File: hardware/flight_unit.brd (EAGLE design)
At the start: 160 x 100 mm, 28 parts, among them IC2 7805T, J2 CONN_20X2SHROUDED, T1 THERMISTOR-2,5, U1 4MB Flash, U2 4MB Flash, U3 4MB Flash, X1 S4B-ZR, X2 S4B-ZR

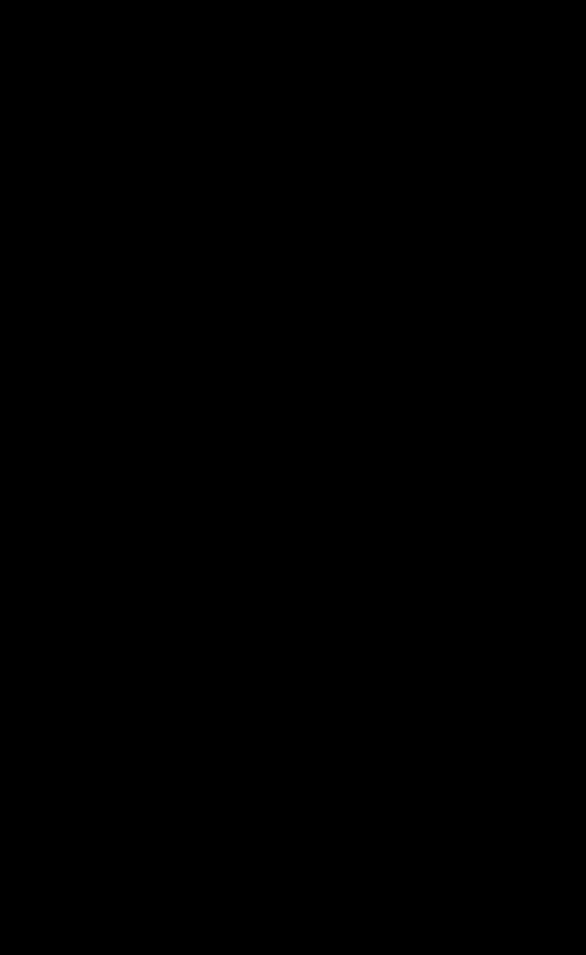
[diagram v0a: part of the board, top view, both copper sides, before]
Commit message: Added decoupling caps to memory schematic
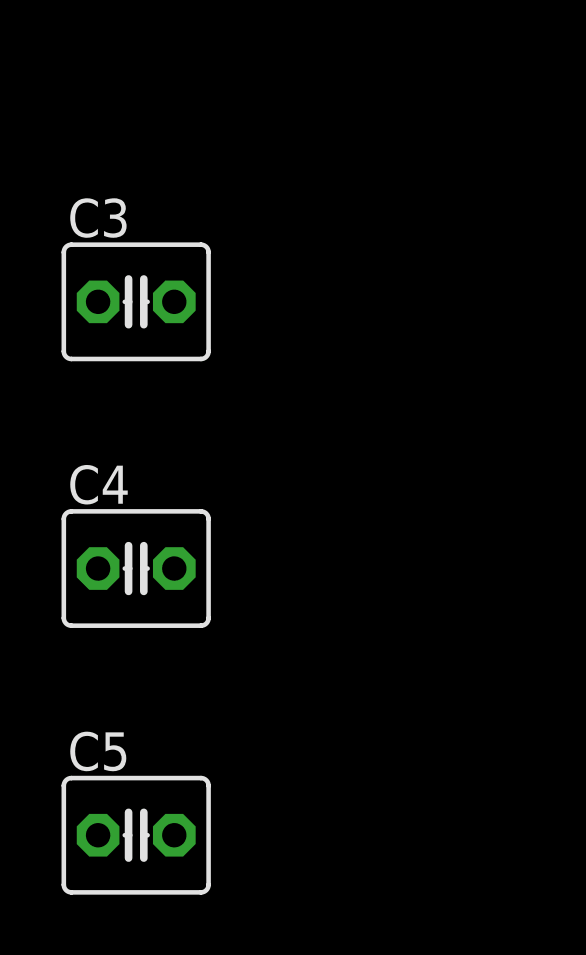
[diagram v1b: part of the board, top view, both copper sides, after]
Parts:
- added C3, C4, C5: 10uF, adafruit:C025-040X050
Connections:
- net +3V3: now also C3.1, C4.1, C5.1
- net GND: now also C3.2, C4.2, C5.2
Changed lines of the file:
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@@
 <attribute name="VALUE" x="-68.58" y="85.09" size="1.27" layer="27"/>
+</element>
+<element name="C3" library="adafruit" library_urn="urn:adsk.eagle:library:420" package="C025-040X050" package3d_urn="urn:adsk.eagle:package:6240321/1" value="10uF" x="-72.39" y="-5.08" smashed="yes">
+<attribute name="NAME" x="-74.676" y="-2.921" size="1.27" layer="25" ratio="10"/>
+<attribute name="VALUE" x="-74.676" y="-8.509" size="1.27" layer="27" ratio="10"/>
+</element>
+<element name="C4" library="adafruit" library_urn="urn:adsk.eagle:library:420" package="C025-040X050" package3d_urn="urn:adsk.eagle:package:6240321/1" value="10uF" x="-72.39" y="-13.97" smashed="yes">
+<attribute name="NAME" x="-74.676" y="-11.811" size="1.27" layer="25" ratio="10"/>
+<attribute name="VALUE" x="-74.676" y="-17.399" size="1.27" layer="27" ratio="10"/>
+</element>
+<element name="C5" library="adafruit" library_urn="urn:adsk.eagle:library:420" package="C025-040X050" package3d_urn="urn:adsk.eagle:package:6240321/1" value="10uF" x="-72.39" y="-22.86" smashed="yes">
+<attribute name="NAME" x="-74.676" y="-20.701" size="1.27" layer="25" ratio="10"/>
+<attribute name="VALUE" x="-74.676" y="-26.289" size="1.27" layer="27" ratio="10"/>
 </element>
 </elements>
@@
 <contactref element="R8" pad="1"/>
 <contactref element="U$3" pad="VIN"/>
+<contactref element="C3" pad="1"/>
+<contactref element="C4" pad="1"/>
+<contactref element="C5" pad="1"/>
 <wire x1="-27.94" y1="121.92" x2="-19.685" y2="118.37" width="0" layer="19" extent="1-1"/>
 <wire x1="-20.19" y1="107.95" x2="-19.685" y2="118.37" width="0" layer="19" extent="1-1"/>
@@
 <wire x1="-48.26" y1="64.77" x2="-70.99" y2="87.63" width="0" layer="19" extent="1-1"/>
 <wire x1="-33.655" y1="64.77" x2="-48.26" y2="64.77" width="0" layer="19" extent="1-1"/>
+<wire x1="-73.66" y1="-5.08" x2="-48.26" y2="64.77" width="0" layer="19" extent="1-1"/>
+<wire x1="-73.66" y1="-13.97" x2="-73.66" y2="-5.08" width="0" layer="19" extent="1-1"/>
+<wire x1="-73.66" y1="-22.86" x2="-73.66" y2="-13.97" width="0" layer="19" extent="1-1"/>
 </signal>
 <signal name="GND">
@@
 <contactref element="RN2" pad="5"/>
 <contactref element="U$3" pad="GND"/>
+<contactref element="C3" pad="2"/>
+<contactref element="C4" pad="2"/>
+<contactref element="C5" pad="2"/>
 <wire x1="-29.21" y1="129.54" x2="-19.05" y2="129.54" width="0" layer="19" extent="1-1"/>
 <wire x1="-31.75" y1="120.65" x2="-29.21" y2="129.54" width="0" layer="19" extent="1-1"/>
@@
 <wire x1="-48.385" y1="5.08" x2="-40.515" y2="5.08" width="0" layer="19" extent="1-1"/>
 <wire x1="-48.385" y1="10.16" x2="-48.385" y2="5.08" width="0" layer="19" extent="1-1"/>
+<wire x1="-71.12" y1="-5.08" x2="-48.385" y2="5.08" width="0" layer="19" extent="1-1"/>
+<wire x1="-71.12" y1="-13.97" x2="-71.12" y2="-5.08" width="0" layer="19" extent="1-1"/>
+<wire x1="-71.12" y1="-22.86" x2="-71.12" y2="-13.97" width="0" layer="19" extent="1-1"/>
 </signal>
 <signal name="N$4">

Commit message: updates to schematic and preliminary board work
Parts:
- removed J2: CONN_20X2SHROUDED, SparkFun-Connectors:2X20_SHROUDED
- removed R2, R3: 1k, resistor:R1210
- added J1: CONN_20X2SHROUDED, SparkFun-Connectors:2X20_SHROUDED
- moved C3 152.1 mm to (68.6, 52.1)
- moved C5 150.6 mm to (64.8, 39.4)
- moved U1 149.0 mm to (68.6, 33.0)
- moved U2 146.8 mm to (57.1, 33.0)
- moved C4 130.2 mm to (49.5, 31.8)
- moved RN2 116.6 mm to (53.3, 74.9), turned to 180 degrees
- moved RN1 113.1 mm to (68.6, 66.0), turned to 180 degrees
- moved JP1 112.5 mm to (69.8, 88.9), turned to 90 degrees
- moved U3 111.1 mm to (68.6, 45.7)
- moved C2 106.7 mm to (-160.0, 110.5)
- moved D1 106.7 mm to (-134.6, 119.4)
- moved LED0 106.7 mm to (-174.0, 125.7)
- moved LED1 106.7 mm to (-127.0, 133.3)
- moved R1 106.7 mm to (-160.0, 124.5)
- moved R5 106.7 mm to (-134.6, 111.8)
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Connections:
- removed net N$3: R2.1, U3.7
- removed net N$5: R4.1, U1.7
- removed net N$6: R3.1, U2.7
- new net HOLD_PUP: R4.1, U1.7, U2.7, U3.7
- net +3V3: no longer R2.2, R3.2
- net GND: now also J1.10, J1.13, J1.19, J1.26, J1.29, J1.33, J1.40, J1.5; no longer J2.14, J2.20, J2.25, J2.30, J2.34, J2.39, J2.6, J2.9
- net IIC_SCL: now also J1.30; no longer J2.29
- net IIC_SDA: now also J1.8; no longer J2.7
- net SC_3V3: now also J1.18, J1.2; no longer J2.1, J2.17
- net SC_5V0: now also J1.1, J1.3; no longer J2.2, J2.4
- net SC_D0: now also J1.7; no longer J2.8
- net SC_D1: now also J1.11; no longer J2.12
- net SC_D2: now also J1.15; no longer J2.16
- net SC_D3: now also J1.21; no longer J2.22
- net SC_D4: now also J1.35; no longer J2.36

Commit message: working on board layout
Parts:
- added H1, H2: SEW_HOLE, SparkFun-Retired:SIMPLE_HOLE
- moved R8 238.7 mm to (64.8, 58.4), turned to 270 degrees
- moved X1 226.6 mm to (47.0, 8.89)
- moved R1 224.3 mm to (33.0, 10.2), turned to 180 degrees
- moved D2 213.5 mm to (33.0, 5.08)
- moved C2 210.7 mm to (27.9, 15.2), turned to 90 degrees
- moved X2 208.0 mm to (17.8, 8.89)
- moved LED0 205.1 mm to (7.62, 30.5)
- moved T1 202.0 mm to (57.1, 58.4), turned to 270 degrees
- moved C1 201.6 mm to (27.9, 22.9), turned to 270 degrees
- moved LED2 184.9 mm to (16.5, 30.5)
- moved LED1 183.9 mm to (25.4, 30.5)
- moved D1 182.9 mm to (14.0, 12.7), turned to 180 degrees
- moved R7 179.8 mm to (17.8, 40.6), flipped to the bottom
- moved R6 171.5 mm to (17.8, 47.0), flipped to the bottom
- moved R5 162.8 mm to (17.8, 54.6), flipped to the bottom
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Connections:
- net GND: now also H1.P$1, H2.P$1
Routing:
- net +3V3: track 0.00 -> 167.1 mm
- net N$2: track 0.00 -> 23.7 mm
- net SC_A3: track 0.00 -> 23.3 mm
- net T_0: track 0.00 -> 23.2 mm
- net T_1: track 0.00 -> 19.8 mm
- net N$1: track 0.00 -> 16.6 mm
- net N$4: track 0.00 -> 8.22 mm
- net V_1: track 0.00 -> 4.83 mm
- net A_3: track 0.00 -> 4.83 mm
- net A_2: track 0.00 -> 4.83 mm
- net A_1: track 0.00 -> 4.83 mm
- net A_0: track 0.00 -> 4.83 mm
- added copper zone on layer 1, net GND
- added copper zone on layer 16, net GND
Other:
- board size 160 x 100 mm -> 77.5 x 74.6 mm

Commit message: working on routing...
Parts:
- added R2: 1k, resistor:R1210
- moved C3 54.1 mm to (11.4, 12.7), flipped to the bottom
- moved U1 45.5 mm to (14.0, 29.2)
- moved C1 44.5 mm to (72.4, 20.3)
- moved C2 44.5 mm to (72.4, 12.7)
- moved IC2 44.5 mm to (55.9, 17.8)
- moved C5 33.6 mm to (48.3, -16.5)
- moved U$3 32.5 mm to (27.9, 35.6), turned to 90 degrees
- moved LED2 31.3 mm to (3.56, 58.9), turned to 270 degrees
- moved U3 30.5 mm to (25.4, 20.3)
- moved LED1 29.5 mm to (3.05, 49.8), turned to 270 degrees
- moved D1 25.5 mm to (39.4, 10.2)
- moved X2 25.5 mm to (43.2, 6.35)
- moved C4 25.3 mm to (20.3, 8.89), turned to 180 degrees
- moved D2 21.6 mm to (54.6, 5.08)
- moved R1 21.6 mm to (54.6, 10.2)
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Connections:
- new net HOLD_PUP2: R2.1
- net +3V3: now also R2.2
- net LED_0: now also U$1.7; no longer U$1.5
- net LED_2: now also U$1.5; no longer U$1.7
- net SC_D0: now also U$1.2; no longer U$1.0/RX
- net SC_D2: now also U$1.0/RX; no longer U$1.2
- net T_0: now also U$1.17/A3; no longer U$1.14/A0
- net V_0: now also U$1.14/A0; no longer U$1.16/A2
- net V_1: now also U$1.16/A2; no longer U$1.17/A3
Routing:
- net +3V3: track 167.1 -> 88.7 mm, vias 0 -> 1
- net MEM_SCK: track 0.00 -> 73.7 mm
- net IIC_SDA: track 0.00 -> 59.2 mm
- net SC_3V3: track 0.00 -> 45.6 mm
- net IIC_SCL: track 0.00 -> 44.0 mm
- net MEM_MISO: track 0.00 -> 35.9 mm, vias 0 -> 1
- net MEM_MOSI: track 0.00 -> 34.4 mm
- net V_0: track 0.00 -> 32.8 mm
- net SC_D4: track 0.00 -> 30.5 mm
- net SC_D0: track 0.00 -> 26.6 mm
- net T_1: track 19.8 -> 46.4 mm
- net MEM_CS0: track 0.00 -> 24.7 mm
- net N$2: track 23.7 -> 0.00 mm
- net LED_2: track 0.00 -> 23.2 mm
- net SC_5V0: track 0.00 -> 21.6 mm
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
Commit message: few more tweaks.
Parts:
- moved C5 54.7 mm to (7.11, 19.6)
- moved X1 47.0 mm to (19.1, 7.11)
- moved X2 37.0 mm to (6.60, 11.9), turned to 90 degrees
- moved C3 13.4 mm to (6.35, 25.1)
- moved C4 7.75 mm to (26.9, 13.0)
- moved D1 3.05 mm to (39.4, 13.2)
- moved R2 2.05 mm to (6.35, 31.0), flipped to the top, turned to 180 degrees
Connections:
- net HOLD_PUP: no longer U1.7
- net HOLD_PUP2: now also U1.7
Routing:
- net +3V3: track 88.7 -> 130.5 mm
- net HOLD_PUP2: track 0.00 -> 9.49 mm

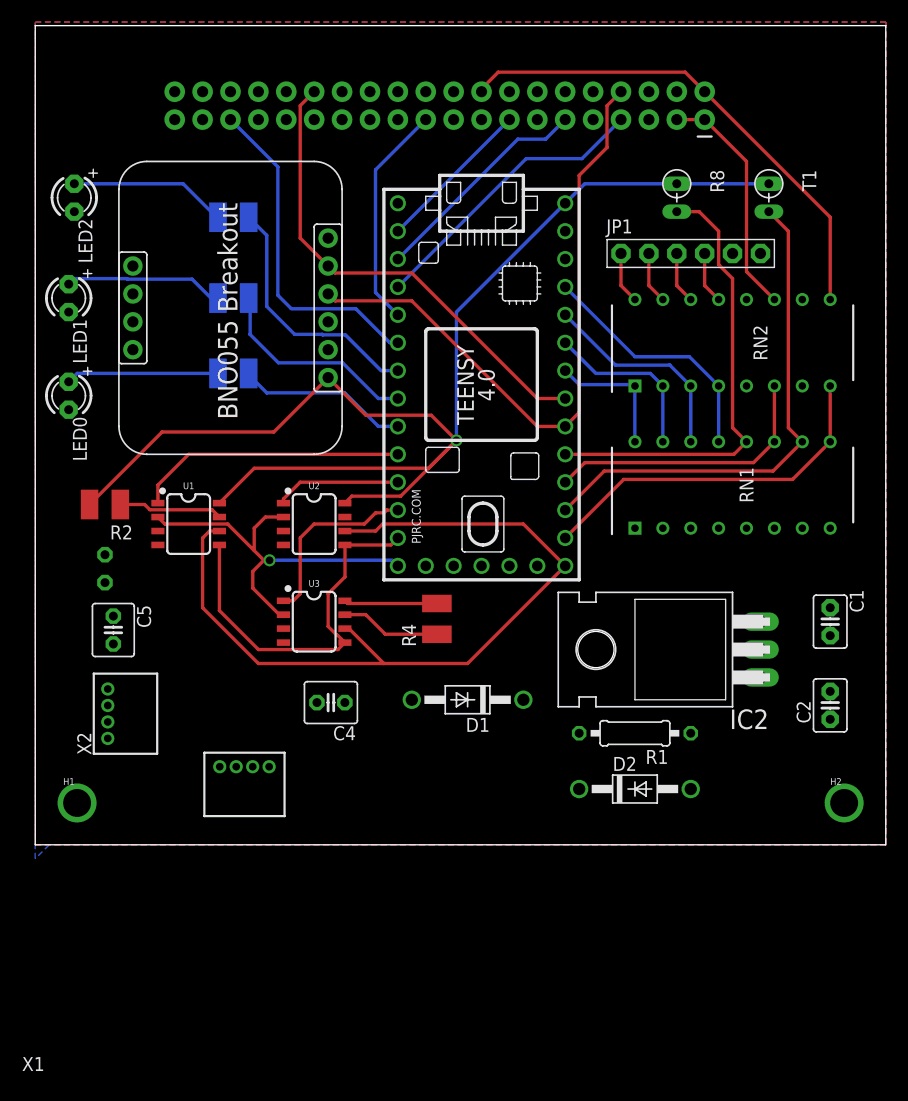
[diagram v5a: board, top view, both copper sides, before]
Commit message: finalized preliminary routing
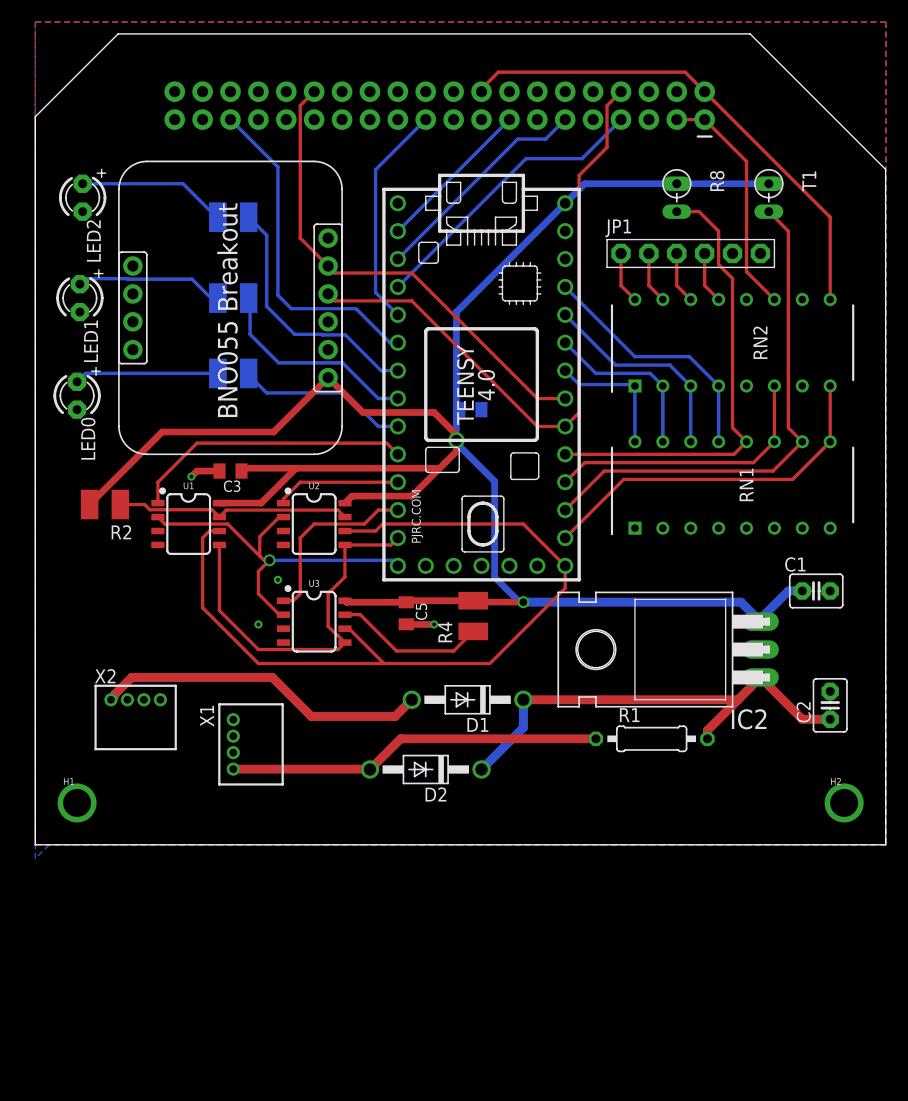
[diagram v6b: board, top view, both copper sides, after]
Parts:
- C3: value 10uF -> 10 uF; device adafruit:C025-040X050 -> adafruit:C0805K
- C4, C5: device adafruit:C025-040X050 -> adafruit:C0805K
- moved C4 29.5 mm to (39.6, 39.6), flipped to the bottom
- moved C5 26.7 mm to (33.8, 21.1)
- moved D2 19.1 mm to (35.6, 6.86), turned to 180 degrees
- moved C3 14.5 mm to (17.8, 34.0), flipped to the top, turned to 180 degrees
- moved R4 3.31 mm to (39.9, 20.8)
- moved C1 3.07 mm to (71.1, 23.1), turned to 0 degrees
- moved X2 2.84 mm to (9.14, 13.2), turned to 0 degrees
- moved X1 2.27 mm to (18.0, 9.14), turned to 90 degrees
- moved R1 1.61 mm to (56.1, 9.65), turned to 0 degrees
- moved LED1 1.02 mm to (4.06, 49.8)
- moved LED0 0.76 mm to (3.81, 40.9)
- moved LED2 0.76 mm to (4.32, 58.9)
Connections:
- net HOLD_PUP: no longer U2.7
- net HOLD_PUP2: now also U2.7
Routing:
- net +3V3: track 130.5 -> 187.8 mm, vias 1 -> 2
- net N$2: track 0.00 -> 43.0 mm
- net N$1: track 0.00 -> 34.2 mm
- net N$4: track 0.00 -> 30.4 mm
- net HOLD_PUP2: track 9.49 -> 21.4 mm
- net GND: track 0.00 -> 5.31 mm, vias 0 -> 4
- net HOLD_PUP: track 9.11 -> 13.8 mm
- net MEM_SCK: track 73.7 -> 74.9 mm
- net MEM_MISO: track 35.9 -> 34.9 mm
- net N$8: track 14.5 -> 13.5 mm
- net MEM_CS0: track 24.7 -> 25.6 mm
- net N$7: track 13.9 -> 13.1 mm
- net N$13: track 14.3 -> 13.6 mm
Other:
- board size 77.5 x 74.6 mm -> 77.5 x 73.8 mm

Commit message: updates before purchase order
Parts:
- removed R1: 3.3k, rcl:0207/10
- removed X1, X2: S4B-ZR, con-jst:S4B-ZR
- added BATTERY, SUPPLY: (no value), adafruit:JST-PH-2-THM
- added R3: 1k, adafruit:R0805
- C1: value 0.1uf -> 1 uF; device capacitor-wima:C2.5-3 -> adafruit:C0805K
- C2: value 0.1uf -> .1 uF; device capacitor-wima:C2.5-3 -> adafruit:C0805K
- R2, R4, R5, R6: device resistor:R1210 -> adafruit:R0805
- R7: value 1k -> 2.2k; device resistor:R1210 -> adafruit:R0805
- moved R7 52.2 mm to (55.6, 6.73), flipped to the top
- moved R2 34.6 mm to (38.4, 17.9), turned to 90 degrees
- moved R4 33.4 mm to (7.62, 29.3)
- moved R6 10.3 mm to (17.8, 39.5), turned to 180 degrees
- moved R5 8.77 mm to (17.8, 48.4), turned to 180 degrees
- moved D2 6.63 mm to (29.0, 7.49)
- moved C1 4.76 mm to (71.9, 18.4), turned to 90 degrees
- moved LED0 3.22 mm to (4.32, 37.7)
- moved C4 3.18 mm to (39.6, 36.4)
- moved U$3 3.18 mm to (27.9, 32.4)
- moved C3 3.18 mm to (17.8, 30.9)
- moved C5 3.18 mm to (33.8, 17.9)
- moved IC2 3.18 mm to (55.9, 14.6)
- moved U1 3.18 mm to (14.0, 26.0)
- moved U2 3.18 mm to (25.4, 26.0)
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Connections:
- removed net N$13: LED2.A, R5.2
- new net N$3: LED2.A, R3.1
- net GND: now also BATTERY.2, SUPPLY.2; no longer X1.2, X2.2
- net HOLD_PUP: now also R2.1; no longer R4.1
- net HOLD_PUP2: now also R4.1; no longer R2.1
- net LED_0: now also R6.2; no longer R7.1
- net LED_1: now also R5.2; no longer R6.1
- net LED_2: now also R3.2; no longer R5.1
- net N$1: now also BATTERY.1, R7.1; no longer R1.1, X1.1
- net N$2: now also R7.2; no longer R1.2
- net N$4: now also SUPPLY.1; no longer X2.1
- net N$7: now also R6.1; no longer R7.2
- net N$8: now also R5.1; no longer R6.2
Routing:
- net N$3: track 0.00 -> 13.8 mm
- net N$13: track 13.6 -> 0.00 mm
- net N$1: track 34.2 -> 42.6 mm
- net N$2: track 43.0 -> 49.2 mm
- net +3V3: track 187.8 -> 184.9 mm
- net HOLD_PUP: track 13.8 -> 12.8 mm
- net LED_1: track 19.2 -> 19.9 mm
- net LED_2: track 23.2 -> 23.7 mm
- net N$8: track 13.5 -> 13.0 mm
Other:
- board size 77.5 x 73.8 mm -> 77.5 x 70.7 mm
